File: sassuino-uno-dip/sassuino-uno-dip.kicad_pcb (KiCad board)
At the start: 2 copper layers, 68.6 x 53.3 mm, 33 parts, among them J1 USB_B, J10 OSCPWR_HDR, J2 POWER2_HDR, J3 ICSP_HDR, J4 POWER_HDR, J5 PORTC_HDR, J6 PORTB_HDR, J7 PORTD_HDR, J8 XTAL2_HDR, J9 XTAL1_HDR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

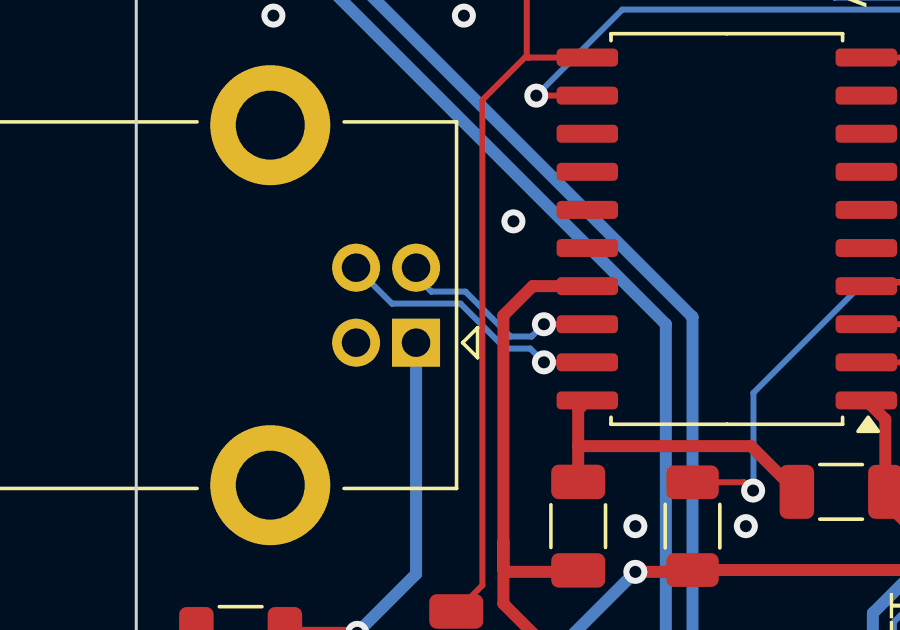
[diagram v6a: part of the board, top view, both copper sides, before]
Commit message: Equalize length of differential usb traces.
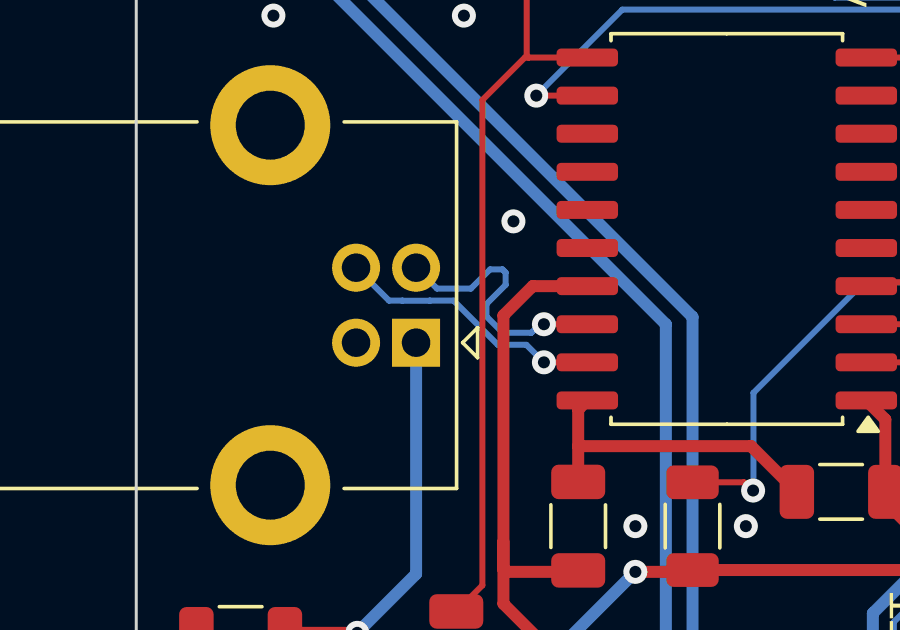
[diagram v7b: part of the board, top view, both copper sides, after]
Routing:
- net /D-: track 6.43 -> 9.02 mm
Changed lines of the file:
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@@
 	)
 	(segment
-		(start 60.635 118.928)
-		(end 60.325 118.618)
+		(start 61.5188 118.8266)
+		(end 61.95675 118.8266)
 		(width 0.2)
 		(layer "B.Cu")
@@
 	)
 	(segment
-		(start 61.772902 118.928)
-		(end 60.635 118.928)
+		(start 61.95675 118.8266)
+		(end 62.596375 118.186976)
 		(width 0.2)
 		(layer "B.Cu")
@@
 	)
 	(segment
-		(start 63.269901 120.424999)
-		(end 61.772902 118.928)
+		(start 60.8241 118.8266)
+		(end 61.5188 118.8266)
 		(width 0.2)
 		(layer "B.Cu")
@@
 	)
 	(segment
-		(start 64.389 120.015)
-		(end 63.979001 120.424999)
+		(start 64.2557 120.015)
+		(end 64.389 120.015)
 		(width 0.2)
 		(layer "B.Cu")
@@
 	)
 	(segment
-		(start 63.979001 120.424999)
-		(end 63.269901 120.424999)
+		(start 62.596375 118.186976)
+		(end 63.009325 118.186975)
+		(width 0.2)
+		(layer "B.Cu")
+		(net 4)
+	)
+	(segment
+		(start 63.9709 120.2998)
+		(end 64.2557 120.015)
+		(width 0.2)
+		(layer "B.Cu")
+		(net 4)
+	)
+	(segment
+		(start 63.112562 118.703162)
+		(end 62.472938 119.342787)
+		(width 0.2)
+		(layer "B.Cu")
+		(net 4)
+	)
+	(segment
+		(start 63.112562 118.290212)
+		(end 63.112562 118.703162)
+		(width 0.2)
+		(layer "B.Cu")
+		(net 4)
+	)
+	(segment
+		(start 62.472937 119.755737)
+		(end 63.017 120.2998)
+		(width 0.2)
+		(layer "B.Cu")
+		(net 4)
+	)
+	(segment
+		(start 62.472938 119.342787)
+		(end 62.472937 119.755737)
+		(width 0.2)
+		(layer "B.Cu")
+		(net 4)
+	)
+	(segment
+		(start 63.9572 120.2998)
+		(end 63.9709 120.2998)
+		(width 0.2)
+		(layer "B.Cu")
+		(net 4)
+	)
+	(segment
+		(start 63.017 120.2998)
+		(end 63.9572 120.2998)
+		(width 0.2)
+		(layer "B.Cu")
+		(net 4)
+	)
+	(segment
+		(start 63.009325 118.186975)
+		(end 63.112562 118.290212)
+		(width 0.2)
+		(layer "B.Cu")
+		(net 4)
+	)
+	(segment
+		(start 60.1275 118.13)
+		(end 60.8241 118.8266)
 		(width 0.2)
 		(layer "B.Cu")
@@
 	)
 	(segment
-		(start 61.606802 119.329)
-		(end 59.3265 119.329)
+		(start 59.2251 119.2276)
+		(end 58.1275 118.13)
 		(width 0.2)
 		(layer "B.Cu")
@@
 	)
 	(segment
-		(start 63.103801 120.825999)
-		(end 61.606802 119.329)
+		(start 60.58355 119.231)
+		(end 59.67145 119.231)
 		(width 0.2)
 		(layer "B.Cu")
@@
 	)
 	(segment
+		(start 59.67145 119.231)
+		(end 59.66805 119.2276)
+		(width 0.2)
+		(layer "B.Cu")
+		(net 35)
+	)
+	(segment
+		(start 63.8048 120.7008)
+		(end 62.8509 120.7008)
+		(width 0.2)
+		(layer "B.Cu")
+		(net 35)
+	)
+	(segment
 		(start 64.389 121.285)
-		(end 63.929999 120.825999)
+		(end 63.8048 120.7008)
 		(width 0.2)
 		(layer "B.Cu")
@@
 	)
 	(segment
-		(start 63.929999 120.825999)
-		(end 63.103801 120.825999)
+		(start 62.8509 120.7008)
+		(end 61.3777 119.2276)
 		(width 0.2)
 		(layer "B.Cu")
@@
 	)
 	(segment
-		(start 59.3265 119.329)
-		(end 58.1275 118.13)
+		(start 59.66805 119.2276)
+		(end 59.2251 119.2276)
+		(width 0.2)
+		(layer "B.Cu")
+		(net 35)
+	)
+	(segment
+		(start 61.3777 119.2276)
+		(end 60.58695 119.2276)
+		(width 0.2)
+		(layer "B.Cu")
+		(net 35)
+	)
+	(segment
+		(start 60.58695 119.2276)
+		(end 60.58355 119.231)
 		(width 0.2)
 		(layer "B.Cu")
@@
 		)
 	)
+	(generated
+		(type tuning_pattern)
+		(name "Tuning Pattern")
+		(layer "B.Cu")
+		(base_line
+			(pts
+				(xy 61.5188 118.8266) (xy 61.5438 118.8266) (xy 63.017 120.2998) (xy 63.9572 120.2998)
+			)
+		)
+		(base_line_coupled
+			(pts
+				(xy 62.022122 119.872022) (xy 62.024913 119.874813)
+			)
+		)
+		(corner_radius_percent 80)
+		(end
+			(xy 63.9572 120.2998)
+		)
+		(initial_side "left")
+		(last_diff_pair_gap 0.18)
+		(last_netname "/D-")
+		(last_status "tuned")
+		(last_track_width 0.2)
+		(last_tuning "0.00 mils (tuned)")
+		(max_amplitude 1.92)
+		(min_amplitude 0)
+		(min_spacing 0.73)
+		(origin
+			(xy 61.5188 118.8266)
+		)
+		(override_custom_rules no)
+		(rounded no)
+		(single_sided no)
+		(target_length 1000000)
+		(target_length_max 1000000)
+		(target_length_min 0)
+		(target_skew 0)
+		(target_skew_max 2147.483647)
+		(target_skew_min 0)
+		(tuning_mode "diff_pair_skew")
+		(members "09e830df-8f9d-4ddf-9df1-0d22ff98331f" "1314fa2f-b306-46e1-9bba-c679761d71b2"
+			"4b7077c7-585a-41be-9d29-bf49eeb181a6" "5f023fa4-545e-419f-911c-58c692e14d23"
+			"c31b5855-8751-48c8-a3e5-65969ec96961" "c7399a2a-e66c-4a87-b4d9-5b2f0ca1cfb7"
+			"cc57e954-fe98-46ef-8a77-b250bf6399f3" "db5ee0ea-f58f-4540-9850-5c7082bdf8c4"
+			"de528a6b-c996-4c85-af3e-6f3550d323a9"
+		)
+	)

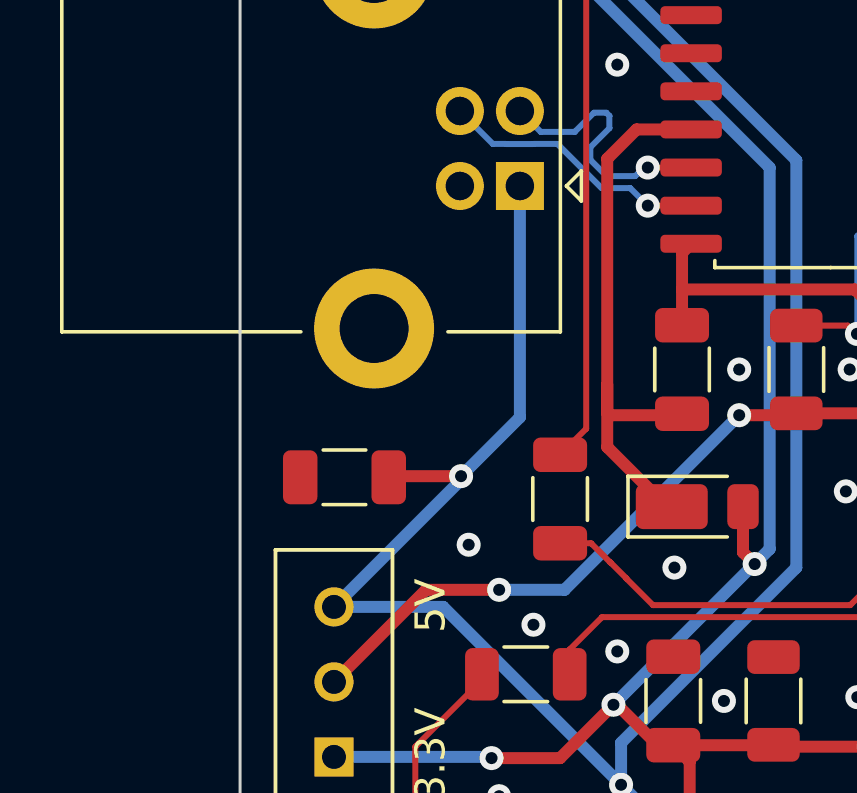
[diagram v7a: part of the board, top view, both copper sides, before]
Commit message: Add a polyfuse on VBUS.
Also ditch the VBUS decoupling cap, I don't recall why I added it.
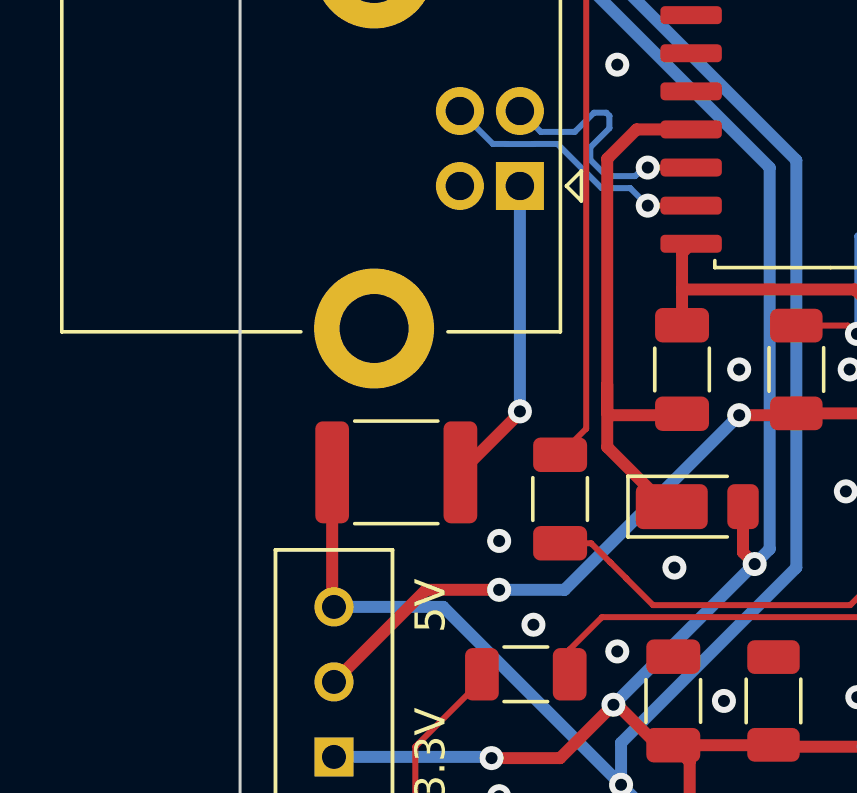
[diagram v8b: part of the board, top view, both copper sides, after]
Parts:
- removed C10: 10uF, Capacitor_SMD:C_1206_3216Metric
- added F1: PTS181216V050, Fuse:Fuse_1812_4532Metric, F.Cu at (56.0, 130.2)
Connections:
- J1 pad 1: +5V -> /VBUS
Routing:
- net +5V: track 122.9 -> 108.4 mm, vias 2 -> 1
- net /VBUS: track 0.00 -> 10.4 mm, vias 0 -> 1
